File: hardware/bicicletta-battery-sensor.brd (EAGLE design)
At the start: 45.7 x 19.1 mm, 18 parts, among them IC1 LMV324MZ

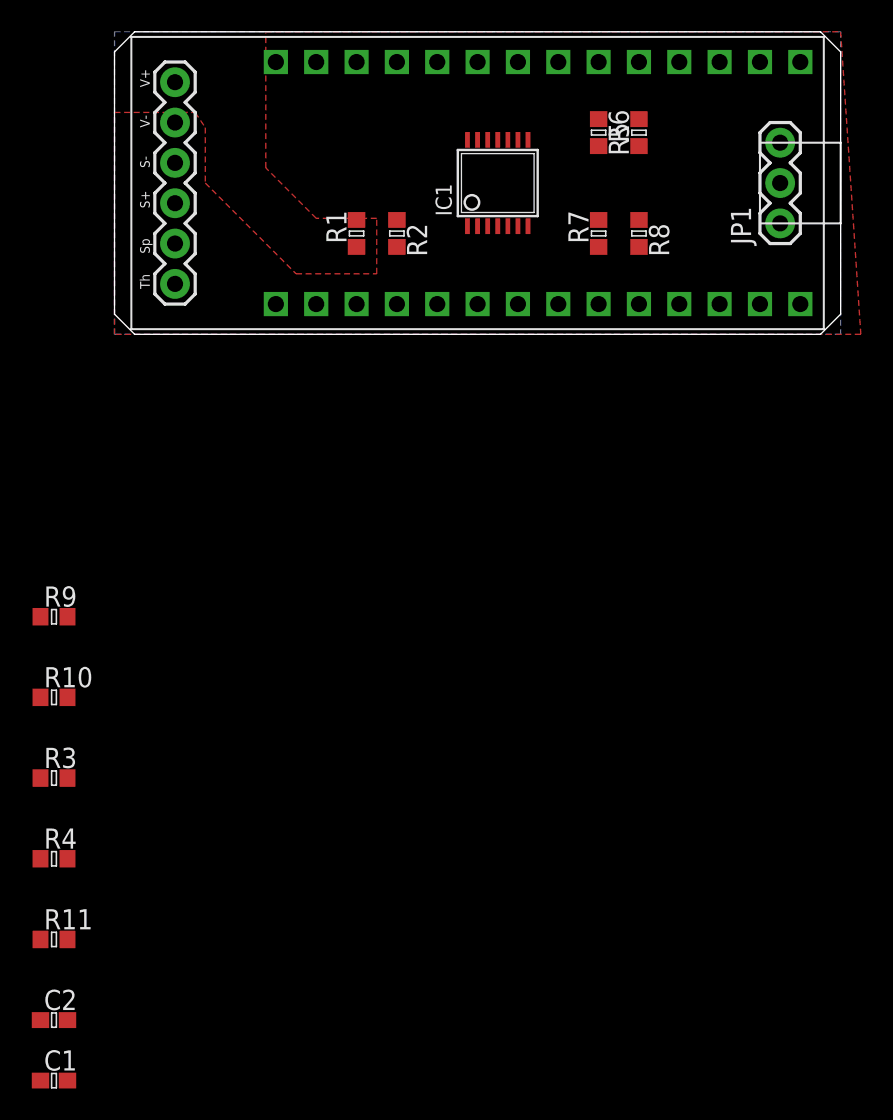
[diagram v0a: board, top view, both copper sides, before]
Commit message: Let's use the LMP92064!
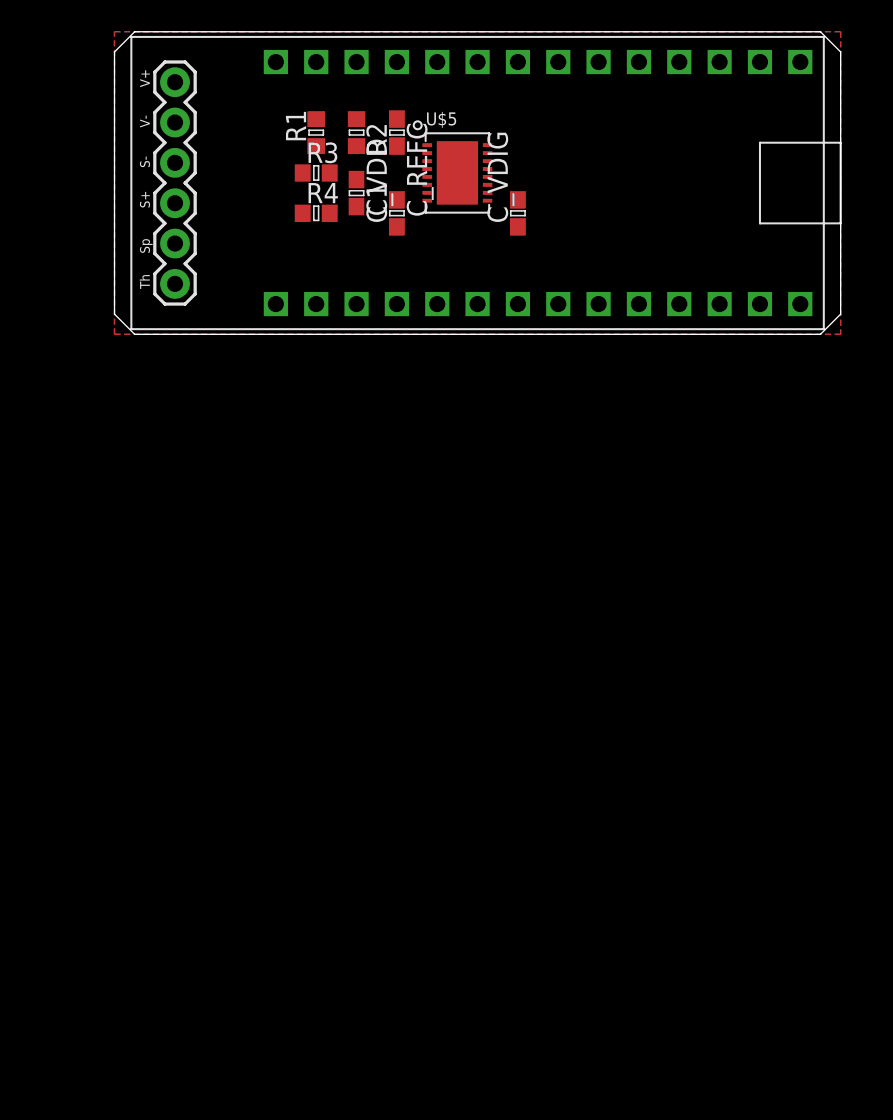
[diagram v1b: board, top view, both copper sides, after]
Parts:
- removed C2: (no value), rcl:C0603
- removed IC1: LMV324MZ, linear:TSSOP14
- removed JP1: (no value), SparkFun-Connectors:1X03
- removed R10, R9: 600, rcl:R0603
- removed R11: 60K, rcl:R0603
- removed R5: 10K, rcl:R0603
- removed R6: 5.8K, rcl:R0603
- removed R7: 1K, rcl:R0603
- removed R8: 2K, rcl:R0603
- added C_REFC: 1uF, rcl:C0603
- added C_VDD, C_VDIG: 0.1uF, rcl:C0603
- added U$5: LMP92064, Railstars:WSON-16
- C1: value 100nF -> 1nF
- R1: value 60K -> 36K5 1%
- R2: value 3K -> 1K 1%
- R3: value 50K -> 100
- R4: value 10K -> 100
- moved C1 59.0 mm to (15.2, 8.89), turned to 270 degrees
- moved R4 43.9 mm to (12.7, 7.62)
- moved R3 41.5 mm to (12.7, 10.2)
- moved R1 6.84 mm to (12.7, 12.7)
- moved R2 6.84 mm to (15.2, 12.7)
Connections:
- removed net BATTERY_3.3: IC1.1, R3.1, U$1.P$23
- removed net BIAS: R4.2, R5.1, R6.2
- removed net N$11: IC1.6, R7.1, R8.2
- removed net THROTTLE_IN_3.3: IC1.5, IC1.7, U$1.P$22
- removed net THROTTLE_IN_5: JP1.2, R7.2
- removed net THROTTLE_OUT_3.3: IC1.10
- new net A0: U$1.P$23
- new net A1: U$1.P$22
- new net CLK_5: U$5.P$13
- new net MISO_5: U$5.P$11
- new net MOSI_5: U$5.P$12
- new net N$4: C1.2, R4.2, U$5.P$4
- new net REFC: C_REFC.1, U$5.P$1
- new net SS_5: U$5.P$14
- net 3.3V: no longer R5.2
- net 5V: now also C_VDD.1, C_VDIG.1, U$5.P$8, U$5.P$9; no longer C1.1, IC1.4, JP1.3
- net GND: now also R2.1, U$5.P$10, U$5.P$16, U$5.P$2, U$5.P$6, U$5.P$7; no longer C1.2, IC1.11, JP1.1, R10.1, R2.2, R6.1, R8.1
- net N$1: now also R1.1, R2.2, U$5.P$5; no longer IC1.9, R10.2, R9.1
- net N$2: now also C_REFC.2, C_VDD.2, C_VDIG.2; no longer IC1.3, R1.2, R2.1
- net N$3: now also C1.1, U$5.P$3; no longer IC1.2, R4.1
- net SHUNT+: now also R3.1
- net SHUNT-: now also R4.1
- net THROTTLE_OUT_5: no longer IC1.8, R9.2
- net V_BATT: now also R1.2; no longer R1.1

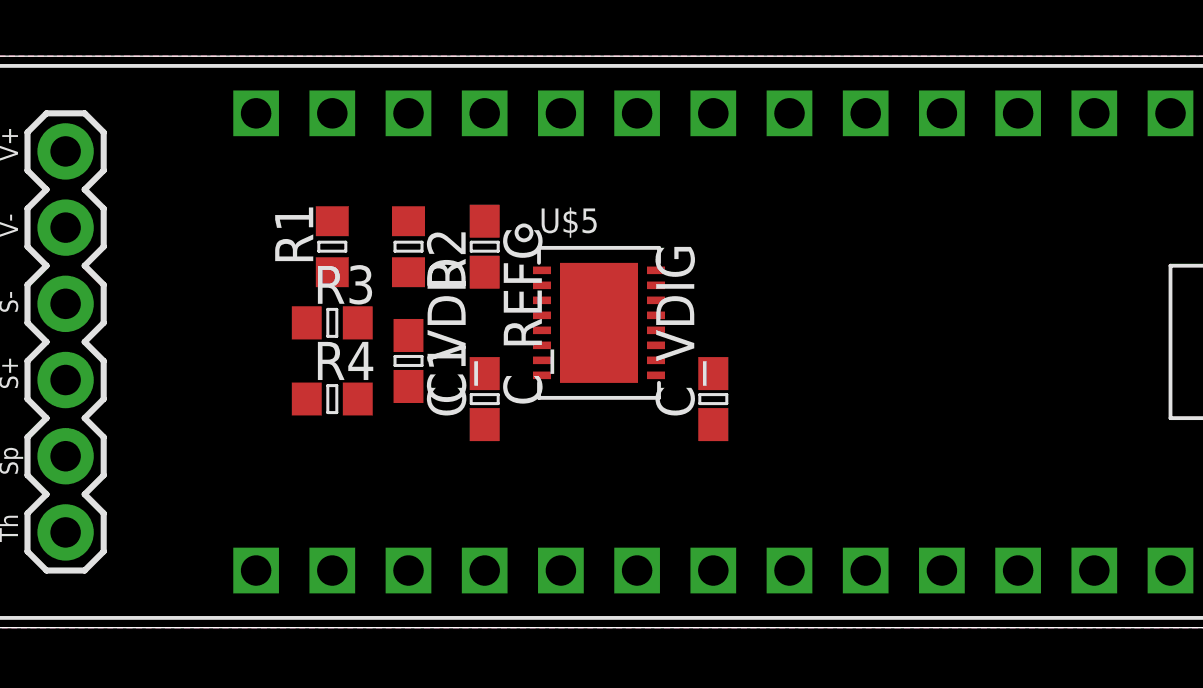
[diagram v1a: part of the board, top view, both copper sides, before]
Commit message: Add level shifter
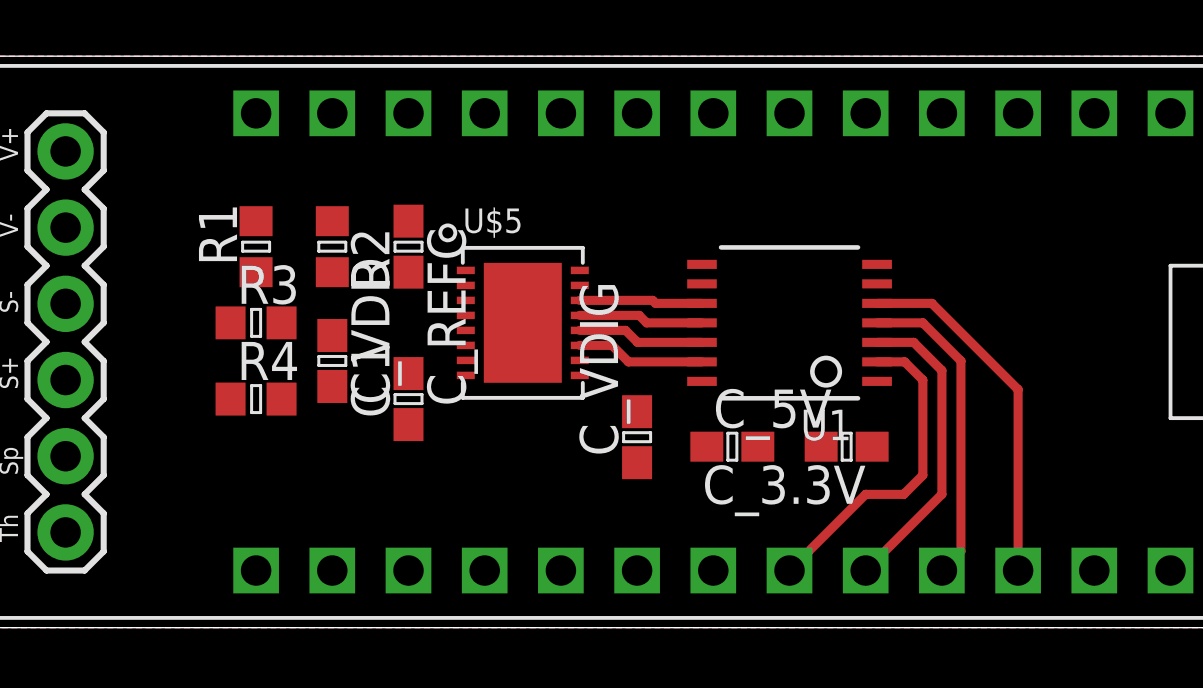
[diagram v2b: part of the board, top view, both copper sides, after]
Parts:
- added C_3.3V, C_5V: 0.1uF, rcl:C0603
- added U1: (no value), adafruit:TSSOP14
- moved C_VDIG 2.84 mm to (22.9, 6.35)
- moved C1 2.54 mm to (12.7, 8.89)
- moved C_REFC 2.54 mm to (15.2, 12.7)
- moved C_VDD 2.54 mm to (15.2, 7.62)
- moved R2 2.54 mm to (12.7, 12.7)
- moved R1 2.54 mm to (10.2, 12.7)
- moved R3 2.54 mm to (10.2, 10.2)
- moved R4 2.54 mm to (10.2, 7.62)
- moved U$5 2.54 mm to (19.1, 10.2)
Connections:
- removed net N$2: C_REFC.2, C_VDD.2, C_VDIG.2
- net 3.3V: now also C_3.3V.1, U1.1, U1.8
- net 5V: now also C_5V.1, U1.14
- net CLK: now also U1.4
- net CLK_5: now also U1.11
- net GND: now also C_3.3V.2, C_5V.2, C_REFC.2, C_VDD.2, C_VDIG.2, U1.7
- net MISO: now also U1.2
- net MISO_5: now also U1.13
- net MOSI: now also U1.3
- net MOSI_5: now also U1.12
- net SS: now also U1.5
- net SS_5: now also U1.10
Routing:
- net SS: track 0.00 -> 11.9 mm
- net MISO: track 0.00 -> 10.7 mm
- net CLK: track 0.00 -> 10.6 mm
- net MOSI: track 0.00 -> 10.3 mm
- net MISO_5: track 0.00 -> 4.30 mm
- net MOSI_5: track 0.00 -> 4.24 mm
- net CLK_5: track 0.00 -> 4.18 mm
- net SS_5: track 0.00 -> 4.11 mm

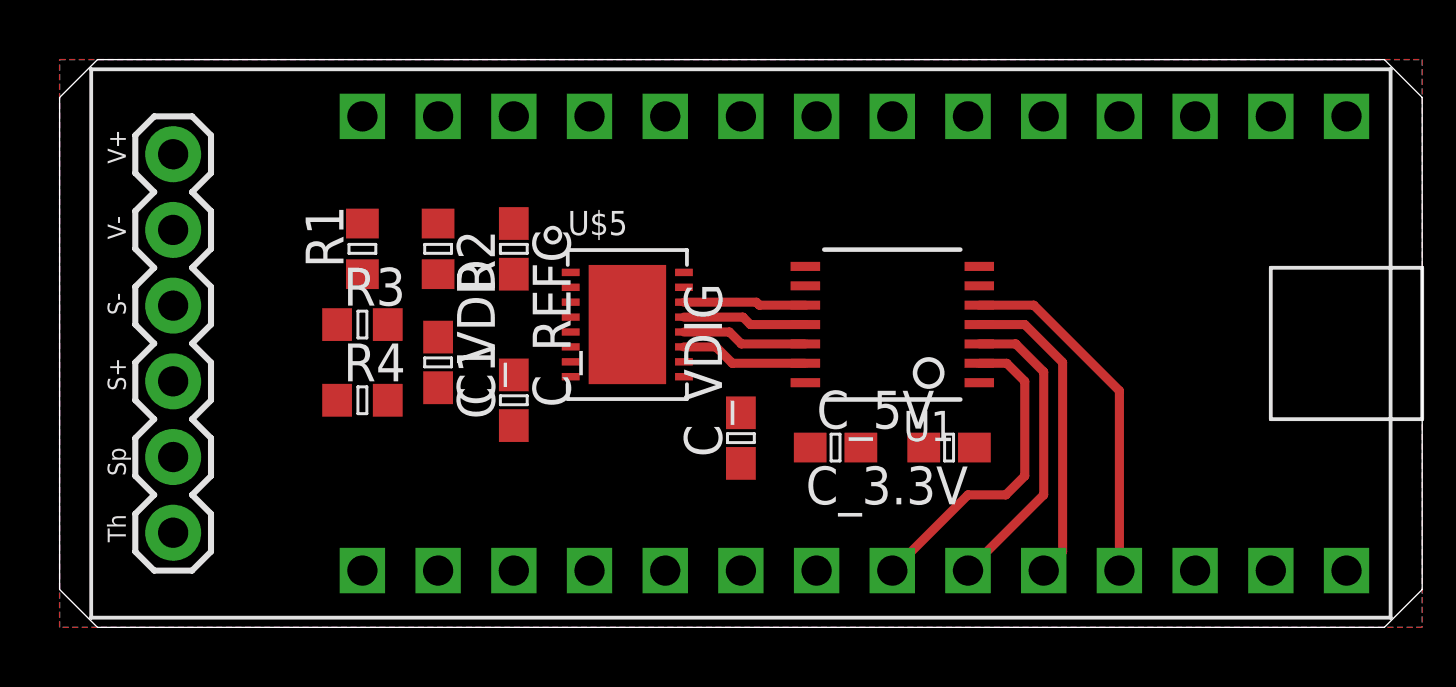
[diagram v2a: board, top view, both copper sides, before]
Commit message: preliminary routing of voltage and current sense PCB
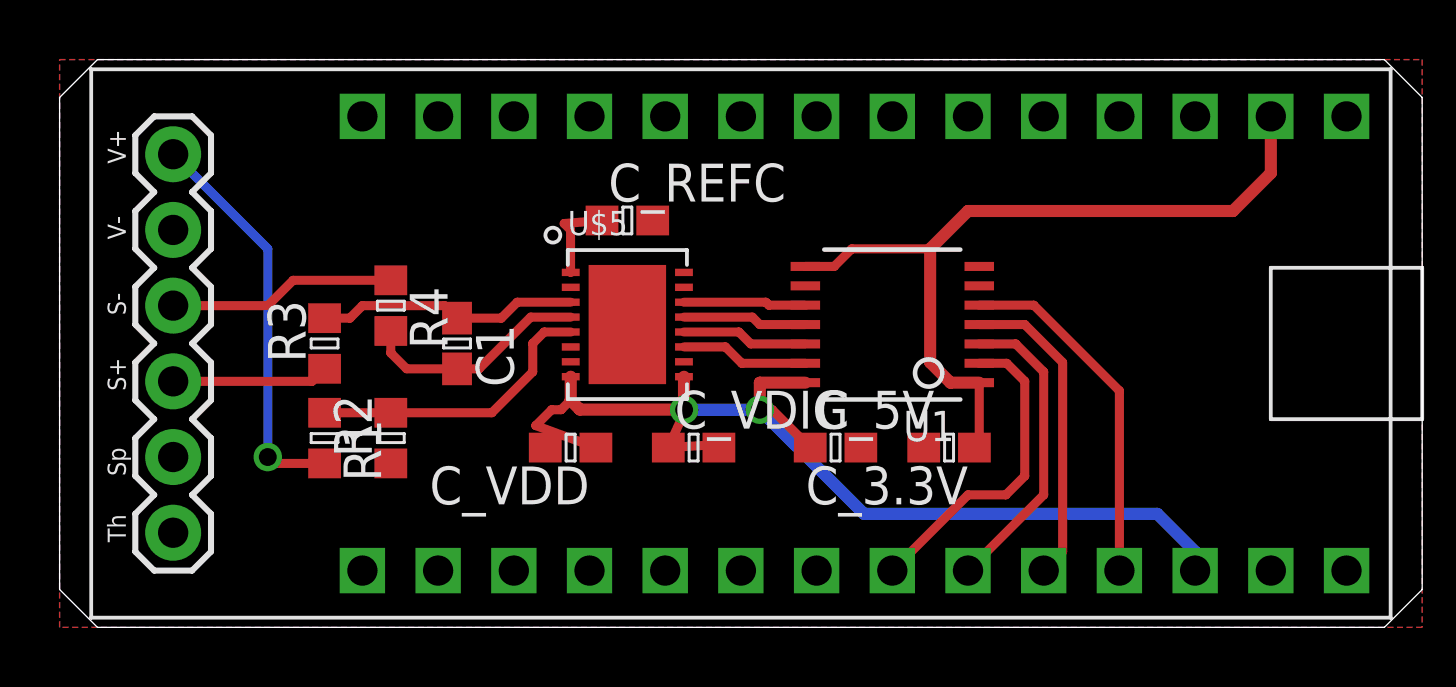
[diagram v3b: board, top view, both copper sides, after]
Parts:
- moved R2 6.55 mm to (11.1, 6.35), turned to 90 degrees
- moved R1 6.48 mm to (8.89, 6.35), turned to 270 degrees
- moved C_REFC 3.93 mm to (19.1, 13.7), turned to 0 degrees
- moved R4 3.31 mm to (11.1, 10.8), turned to 270 degrees
- moved C_VDD 2.48 mm to (17.1, 6.03), turned to 180 degrees
- moved C_VDIG 1.62 mm to (21.3, 6.03), turned to 0 degrees
- moved R3 1.42 mm to (8.89, 9.53), turned to 90 degrees
- moved C1 0.90 mm to (13.3, 9.53)
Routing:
- net 5V: track 0.00 -> 37.0 mm, vias 0 -> 2
- net 3.3V: track 0.00 -> 26.8 mm
- net V_BATT: track 0.00 -> 13.5 mm, vias 0 -> 1
- net N$1: track 0.00 -> 9.94 mm
- net N$3: track 0.00 -> 8.83 mm
- net N$4: track 0.00 -> 7.71 mm
- net SHUNT-: track 0.00 -> 7.65 mm
- net SHUNT+: track 0.00 -> 5.25 mm
- net REFC: track 0.00 -> 3.01 mm

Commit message: Nearly finalized PCB for battery sensor module
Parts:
- moved R1 1.93 mm to (9.21, 8.26)
- moved R2 1.93 mm to (11.4, 8.26)
- moved C1 1.93 mm to (13.7, 11.4)
- moved R3 1.93 mm to (9.21, 11.4)
- moved R4 1.93 mm to (11.4, 12.7)
- renumbered U$5 to IC1, U1 to IC2
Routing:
- net 5V: track 37.0 -> 5.08 mm, vias 2 -> 0
- net GND: track 0.00 -> 18.2 mm, vias 0 -> 9
- net N$1: track 9.94 -> 8.28 mm
- net V_BATT: track 13.5 -> 11.9 mm
- net SHUNT-: track 7.65 -> 8.76 mm
- net SHUNT+: track 5.25 -> 6.36 mm
- net N$4: track 7.71 -> 6.75 mm
- added copper zone on layer 1, net 5V
- removed copper zone on layer 1, net GND
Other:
- board text added: "bicicletta battery sensor"
- board text removed: "bicicletta sensor"

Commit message: Add value to the TXB0108
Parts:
- IC2: value (none) -> TXB0108
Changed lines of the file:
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@@
 <attribute name="VALUE" x="11.7475" y="12.065" size="1.27" layer="27" rot="R270"/>
 </element>
-<element name="IC2" library="adafruit" package="TSSOP14" value="" x="27.94" y="10.16" smashed="yes" rot="R90">
+<element name="IC2" library="adafruit" package="TSSOP14" value="TXB0108" x="27.94" y="10.16" smashed="yes" rot="R90">
 <attribute name="NAME" x="30.0228" y="7.2644" size="0.6096" layer="25" ratio="10" rot="SR180"/>
 <attribute name="VALUE" x="30.0228" y="14.0462" size="1.016" layer="27" ratio="10" rot="R180"/>
